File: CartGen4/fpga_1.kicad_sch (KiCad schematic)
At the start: 5 parts

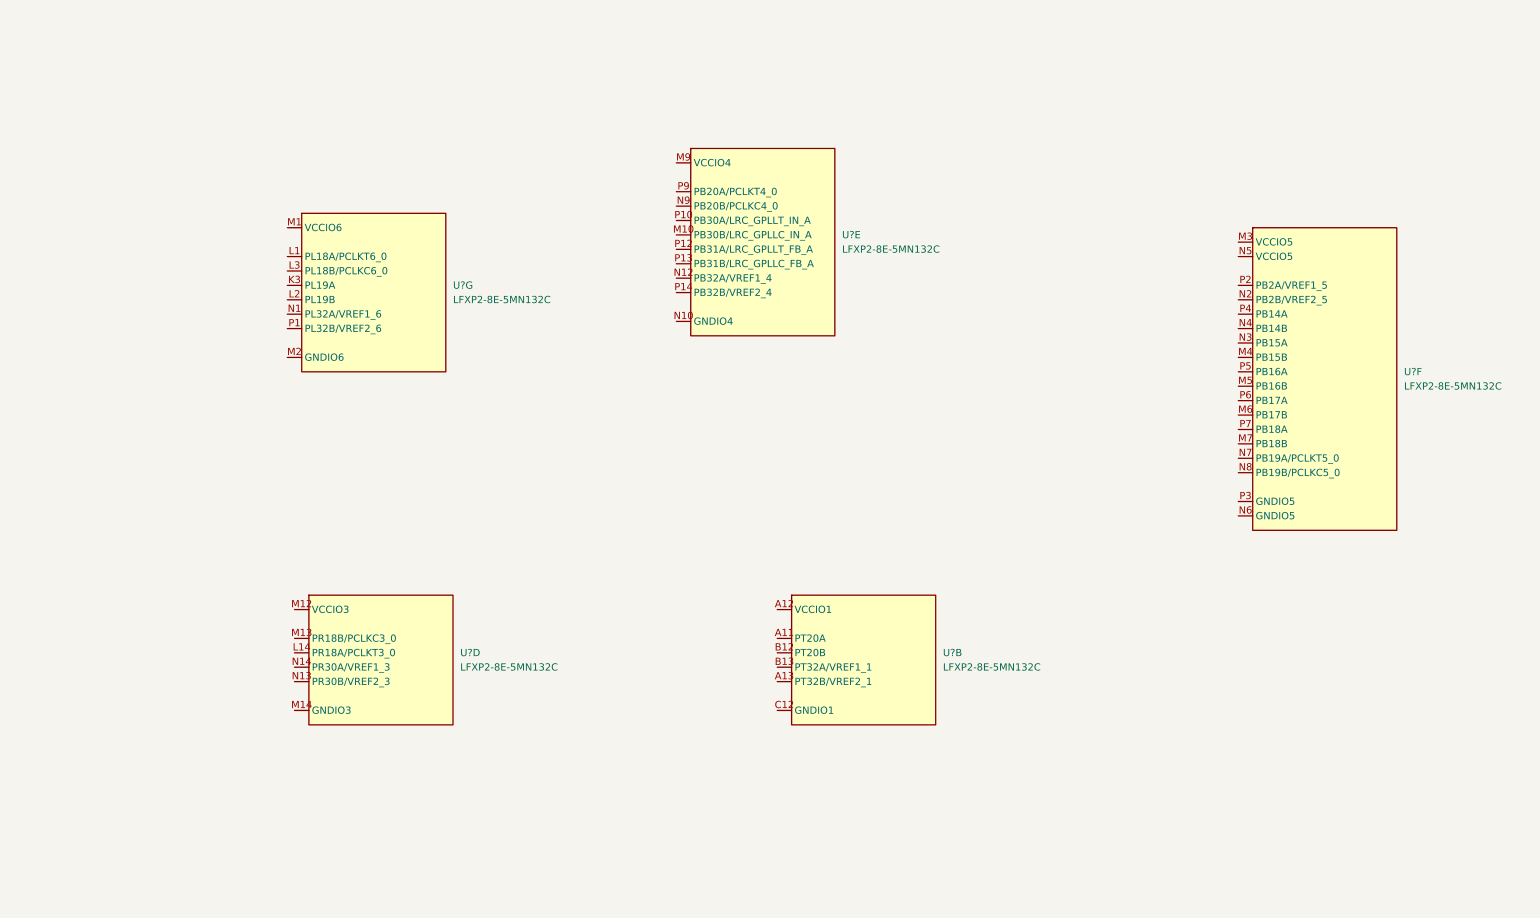
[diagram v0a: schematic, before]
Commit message: Added FPGA <> Gameboy connections
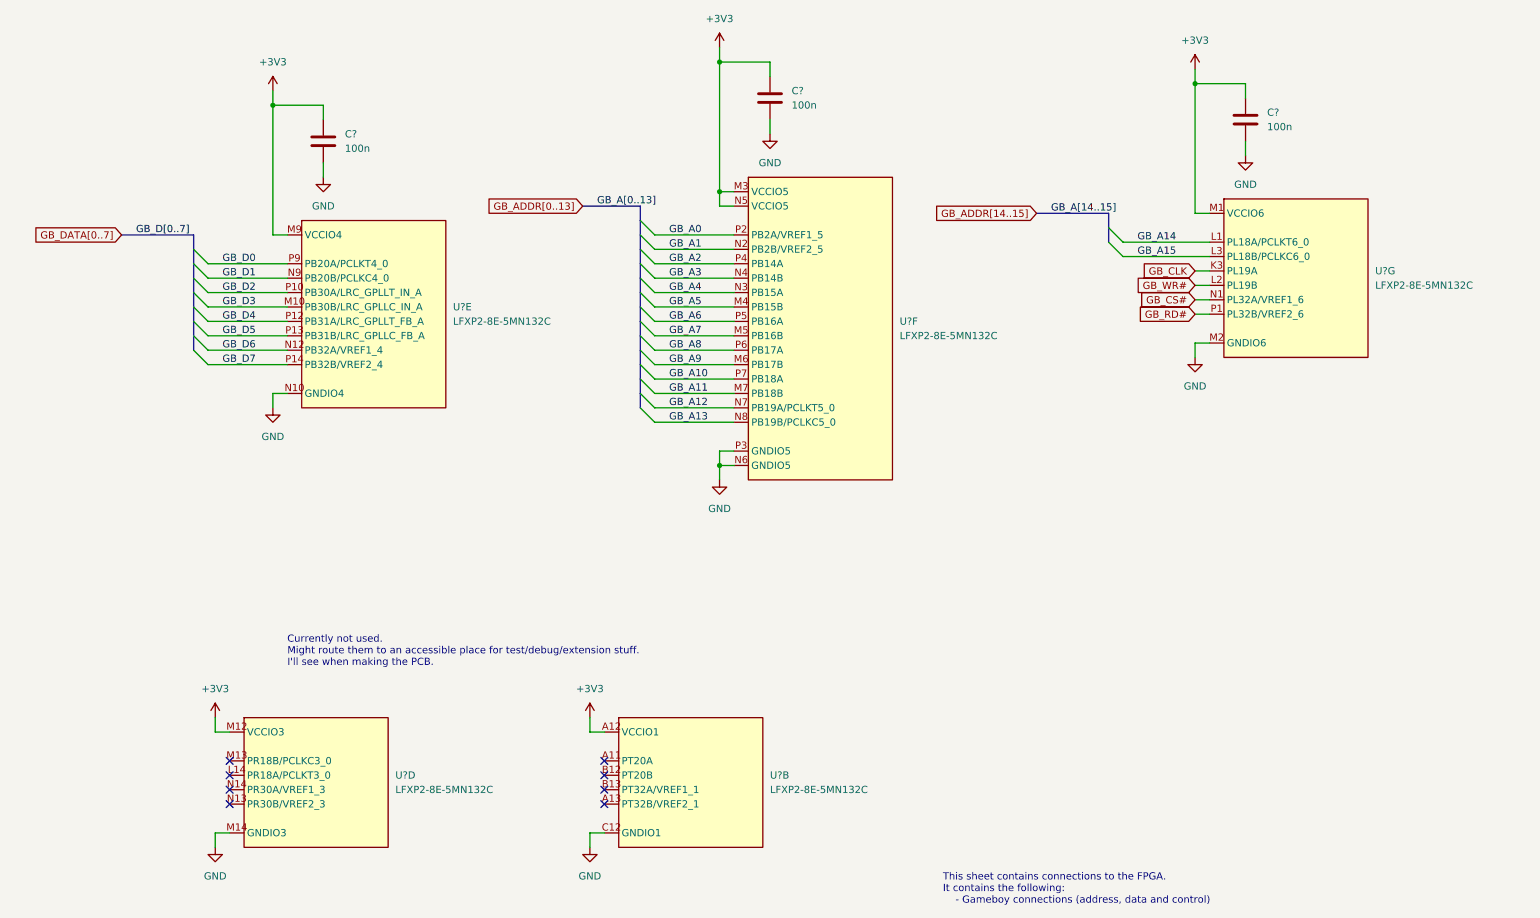
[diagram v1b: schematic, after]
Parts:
- added C? (x3): 100n, symbol Device:C
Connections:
- net +3V3: now reaches U?.M12 (VCCIO3)
- net +3V3: now also U?.A12 (VCCIO1), U?.M1 (VCCIO6), U?.M3 (VCCIO5), U?.M9 (VCCIO4), U?.N5 (VCCIO5), C?.1, C?.1, C?.1
- net GND: now reaches U?.M14 (GNDIO3)
- net GND: now also U?.C12 (GNDIO1), U?.M2 (GNDIO6), U?.N10 (GNDIO4), U?.N6 (GNDIO5), U?.P3 (GNDIO5), C?.2, C?.2, C?.2
- net GB_D3: now reaches U?.M10 (PB30B/LRC_GPLLC_IN_A)
- net GB_D6: now reaches U?.N12 (PB32A/VREF1_4)
- net GB_D1: now reaches U?.N9 (PB20B/PCLKC4_0)
- net GB_D2: now reaches U?.P10 (PB30A/LRC_GPLLT_IN_A)
- net GB_D4: now reaches U?.P12 (PB31A/LRC_GPLLT_FB_A)
- net GB_D5: now reaches U?.P13 (PB31B/LRC_GPLLC_FB_A)
- net GB_D7: now reaches U?.P14 (PB32B/VREF2_4)
- net GB_D0: now reaches U?.P9 (PB20A/PCLKT4_0)
- net GB_A5: now reaches U?.M4 (PB15B)
- net GB_A7: now reaches U?.M5 (PB16B)
- net GB_A9: now reaches U?.M6 (PB17B)
- net GB_A11: now reaches U?.M7 (PB18B)
- net GB_A1: now reaches U?.N2 (PB2B/VREF2_5)
- net GB_A4: now reaches U?.N3 (PB15A)
- net GB_A3: now reaches U?.N4 (PB14B)
- net GB_A12: now reaches U?.N7 (PB19A/PCLKT5_0)
- net GB_A13: now reaches U?.N8 (PB19B/PCLKC5_0)
- net GB_A0: now reaches U?.P2 (PB2A/VREF1_5)
- net GB_A2: now reaches U?.P4 (PB14A)
- net GB_A6: now reaches U?.P5 (PB16A)
- net GB_A8: now reaches U?.P6 (PB17A)
- net GB_A10: now reaches U?.P7 (PB18A)
- net GB_CLK: now reaches U?.K3 (PL19A)
- net GB_A14: now reaches U?.L1 (PL18A/PCLKT6_0)
- net GB_WR#: now reaches U?.L2 (PL19B)
- net GB_A15: now reaches U?.L3 (PL18B/PCLKC6_0)
- net GB_CS#: now reaches U?.N1 (PL32A/VREF1_6)
- net GB_RD#: now reaches U?.P1 (PL32B/VREF2_6)
- no-connect marks 0 -> 8
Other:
- note added: "Currently not used. Might route them to an accessible place for test/debug/extension stuff. I'll see when making the PCB."
- note added: "This sheet contains connections to the FPGA. It contains the following: - Gameboy connections (address, data and control)"
- moved on the sheet: U?B, U?D, U?E, U?F, U?G

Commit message: Added copyright
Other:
- company: (none) -> © Elijah Almeida Coimbra
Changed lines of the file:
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@@
   (title_block
     (title "FPGA connections 1")
+    (company "© Elijah Almeida Coimbra")
   )
   (junction (at 223.52 29.21) (diameter 0) (color 0 0 0 0)

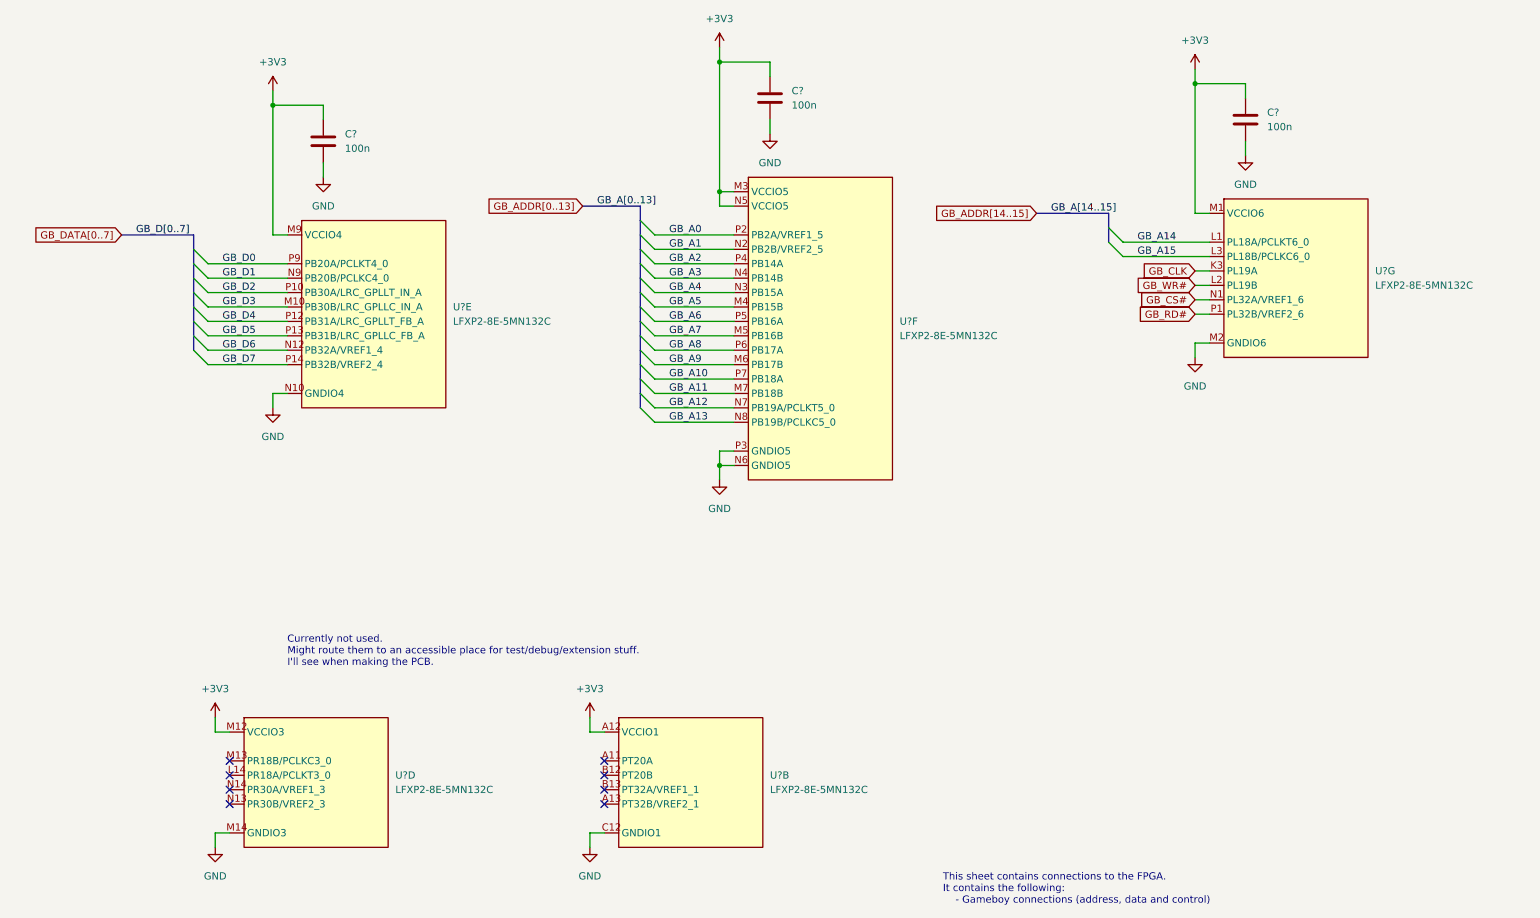
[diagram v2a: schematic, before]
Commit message: Added reference designators to everything
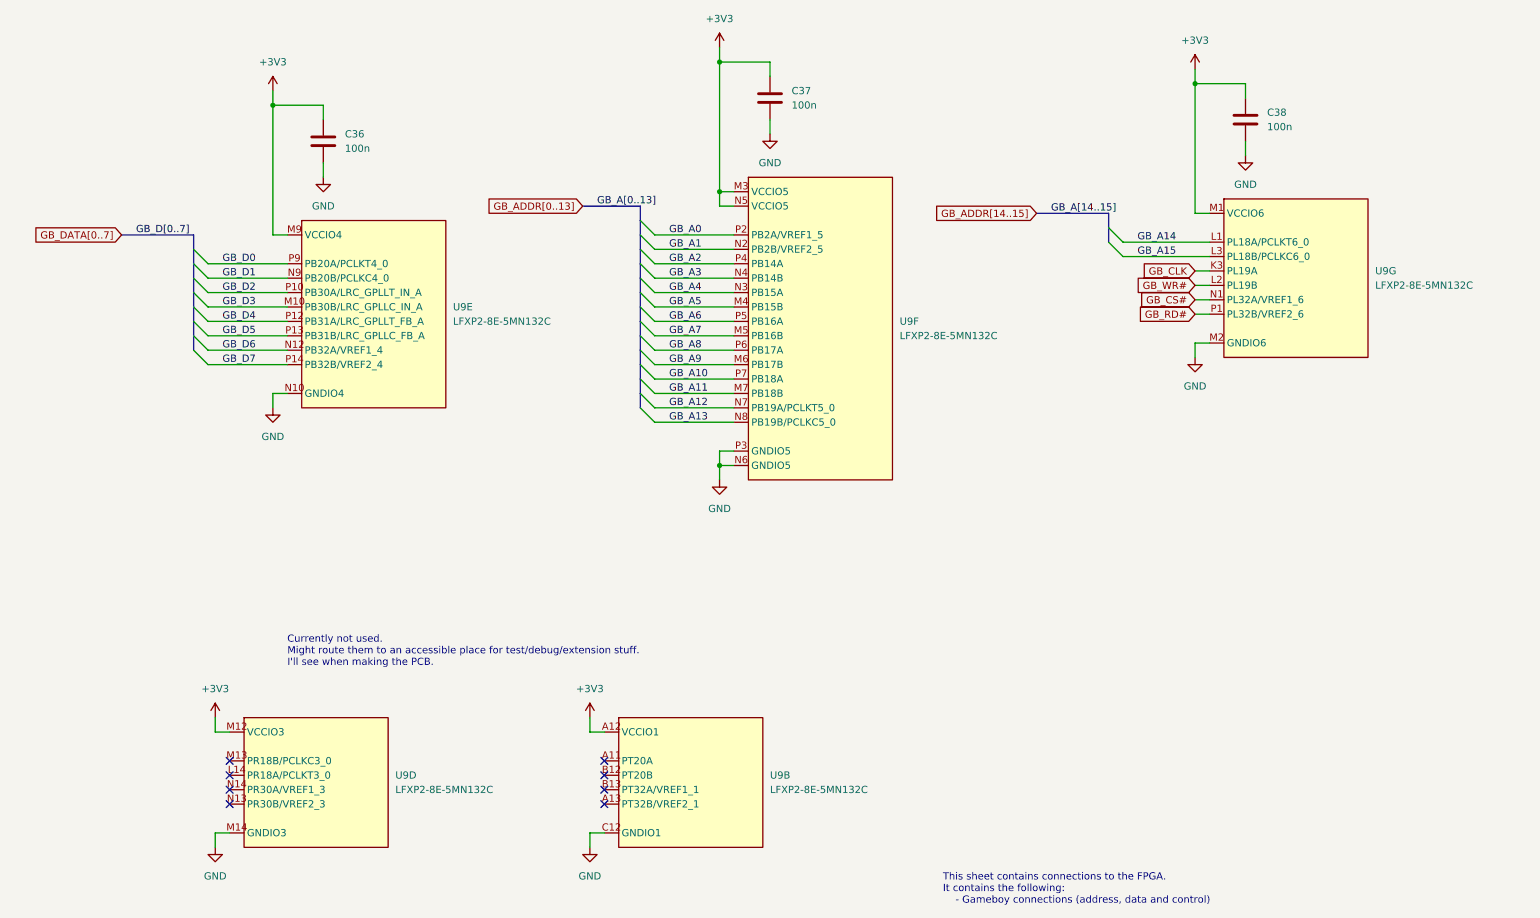
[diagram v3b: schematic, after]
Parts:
- gave numbers to parts that had none: 4
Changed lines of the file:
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@@
   (symbol (lib_id "Device:C") (at 148.59 31.75 0) (unit 1)
     (in_bom yes) (on_board yes) (fields_autoplaced)
-    (property "Reference" "C?" (id 0) (at 152.4 30.4799 0)
+    (property "Reference" "C37" (id 0) (at 152.4 30.4799 0)
       (effects (font (size 1.27 1.27)) (justify left))
     )
@@
   (symbol (lib_id "power:GND") (at 232.41 41.91 0) (unit 1)
     (in_bom yes) (on_board yes) (fields_autoplaced)
-    (property "Reference" "#PWR?" (id 0) (at 232.41 48.26 0)
+    (property "Reference" "#PWR097" (id 0) (at 232.41 48.26 0)
       (effects (font (size 1.27 1.27)) hide)
     )
@@
   (symbol (lib_id "FPGA_Lattice:LFXP2-8E-5MN132C") (at 55.88 140.97 0) (unit 4)
     (in_bom yes) (on_board yes) (fields_autoplaced)
-    (property "Reference" "U?" (id 0) (at 82.55 151.1299 0)
+    (property "Reference" "U9" (id 0) (at 82.55 151.1299 0)
       (effects (font (size 1.27 1.27)) (justify left))
     )
@@
   (symbol (lib_id "power:+3V3") (at 223.52 26.67 0) (unit 1)
     (in_bom yes) (on_board yes) (fields_autoplaced)
-    (property "Reference" "#PWR?" (id 0) (at 223.52 30.48 0)
+    (property "Reference" "#PWR095" (id 0) (at 223.52 30.48 0)
       (effects (font (size 1.27 1.27)) hide)
     )
@@
   (symbol (lib_id "power:+3V3") (at 60.96 30.48 0) (unit 1)
     (in_bom yes) (on_board yes) (fields_autoplaced)
-    (property "Reference" "#PWR?" (id 0) (at 60.96 34.29 0)
+    (property "Reference" "#PWR087" (id 0) (at 60.96 34.29 0)
       (effects (font (size 1.27 1.27)) hide)
     )
@@
   (symbol (lib_id "Device:C") (at 232.41 35.56 0) (unit 1)
     (in_bom yes) (on_board yes) (fields_autoplaced)
-    (property "Reference" "C?" (id 0) (at 236.22 34.2899 0)
+    (property "Reference" "C38" (id 0) (at 236.22 34.2899 0)
       (effects (font (size 1.27 1.27)) (justify left))
     )
@@
   (symbol (lib_id "power:GND") (at 60.96 86.36 0) (unit 1)
     (in_bom yes) (on_board yes) (fields_autoplaced)
-    (property "Reference" "#PWR?" (id 0) (at 60.96 92.71 0)
+    (property "Reference" "#PWR088" (id 0) (at 60.96 92.71 0)
       (effects (font (size 1.27 1.27)) hide)
     )
@@
   (symbol (lib_id "Device:C") (at 69.85 39.37 0) (unit 1)
     (in_bom yes) (on_board yes) (fields_autoplaced)
-    (property "Reference" "C?" (id 0) (at 73.66 38.0999 0)
+    (property "Reference" "C36" (id 0) (at 73.66 38.0999 0)
       (effects (font (size 1.27 1.27)) (justify left))
     )
@@
   (symbol (lib_id "power:+3V3") (at 139.7 22.86 0) (unit 1)
     (in_bom yes) (on_board yes) (fields_autoplaced)
-    (property "Reference" "#PWR?" (id 0) (at 139.7 26.67 0)
+    (property "Reference" "#PWR092" (id 0) (at 139.7 26.67 0)
       (effects (font (size 1.27 1.27)) hide)
     )
@@
   (symbol (lib_id "power:+3V3") (at 116.84 140.97 0) (unit 1)
     (in_bom yes) (on_board yes) (fields_autoplaced)
-    (property "Reference" "#PWR?" (id 0) (at 116.84 144.78 0)
+    (property "Reference" "#PWR090" (id 0) (at 116.84 144.78 0)
       (effects (font (size 1.27 1.27)) hide)
     )
@@
   (symbol (lib_id "power:+3V3") (at 50.8 140.97 0) (unit 1)
     (in_bom yes) (on_board yes) (fields_autoplaced)
-    (property "Reference" "#PWR?" (id 0) (at 50.8 144.78 0)
+    (property "Reference" "#PWR085" (id 0) (at 50.8 144.78 0)
       (effects (font (size 1.27 1.27)) hide)
     )
@@
   (symbol (lib_id "FPGA_Lattice:LFXP2-8E-5MN132C") (at 121.92 140.97 0) (unit 2)
     (in_bom yes) (on_board yes) (fields_autoplaced)
-    (property "Reference" "U?" (id 0) (at 148.59 151.1299 0)
+    (property "Reference" "U9" (id 0) (at 148.59 151.1299 0)
       (effects (font (size 1.27 1.27)) (justify left))
     )
@@
   (symbol (lib_id "power:GND") (at 139.7 99.06 0) (unit 1)
     (in_bom yes) (on_board yes) (fields_autoplaced)
-    (property "Reference" "#PWR?" (id 0) (at 139.7 105.41 0)
+    (property "Reference" "#PWR093" (id 0) (at 139.7 105.41 0)
       (effects (font (size 1.27 1.27)) hide)
     )
@@
   (symbol (lib_id "power:GND") (at 69.85 45.72 0) (unit 1)
     (in_bom yes) (on_board yes) (fields_autoplaced)
-    (property "Reference" "#PWR?" (id 0) (at 69.85 52.07 0)
+    (property "Reference" "#PWR089" (id 0) (at 69.85 52.07 0)
       (effects (font (size 1.27 1.27)) hide)
     )
@@
   (symbol (lib_id "power:GND") (at 148.59 38.1 0) (unit 1)
     (in_bom yes) (on_board yes) (fields_autoplaced)
-    (property "Reference" "#PWR?" (id 0) (at 148.59 44.45 0)
+    (property "Reference" "#PWR094" (id 0) (at 148.59 44.45 0)
       (effects (font (size 1.27 1.27)) hide)
     )
@@
   (symbol (lib_id "power:GND") (at 116.84 163.83 0) (unit 1)
     (in_bom yes) (on_board yes) (fields_autoplaced)
-    (property "Reference" "#PWR?" (id 0) (at 116.84 170.18 0)
+    (property "Reference" "#PWR091" (id 0) (at 116.84 170.18 0)
       (effects (font (size 1.27 1.27)) hide)
     )
@@
   (symbol (lib_id "FPGA_Lattice:LFXP2-8E-5MN132C") (at 66.04 53.34 0) (unit 5)
     (in_bom yes) (on_board yes) (fields_autoplaced)
-    (property "Reference" "U?" (id 0) (at 92.71 68.5799 0)
+    (property "Reference" "U9" (id 0) (at 92.71 68.5799 0)
       (effects (font (size 1.27 1.27)) (justify left))
     )
@@
   (symbol (lib_id "FPGA_Lattice:LFXP2-8E-5MN132C") (at 144.78 45.72 0) (unit 6)
     (in_bom yes) (on_board yes) (fields_autoplaced)
-    (property "Reference" "U?" (id 0) (at 171.45 71.1199 0)
+    (property "Reference" "U9" (id 0) (at 171.45 71.1199 0)
       (effects (font (size 1.27 1.27)) (justify left))
     )
@@
   (symbol (lib_id "power:GND") (at 50.8 163.83 0) (unit 1)
     (in_bom yes) (on_board yes) (fields_autoplaced)
-    (property "Reference" "#PWR?" (id 0) (at 50.8 170.18 0)
+    (property "Reference" "#PWR086" (id 0) (at 50.8 170.18 0)
       (effects (font (size 1.27 1.27)) hide)
     )
@@
   (symbol (lib_id "FPGA_Lattice:LFXP2-8E-5MN132C") (at 228.6 49.53 0) (unit 7)
     (in_bom yes) (on_board yes) (fields_autoplaced)
-    (property "Reference" "U?" (id 0) (at 255.27 62.2299 0)
+    (property "Reference" "U9" (id 0) (at 255.27 62.2299 0)
       (effects (font (size 1.27 1.27)) (justify left))
     )
@@
   (symbol (lib_id "power:GND") (at 223.52 77.47 0) (unit 1)
     (in_bom yes) (on_board yes) (fields_autoplaced)
-    (property "Reference" "#PWR?" (id 0) (at 223.52 83.82 0)
-      (effects (font (size 1.27 1.27)) hide)
-    )
+    (property "Reference" "#PWR096" (id 0) (at 223.52 83.82 0)
+      (effects (font (size 1.27 1.27)) hide)
+    )
